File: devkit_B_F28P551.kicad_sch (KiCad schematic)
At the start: 27 parts, among them J1 DEVKIT_C2000_ROW_A, J2 DEVKIT_C2000_ROW_B, J3 Tag-Connect-2050_10, J4 RESET, U1 TMS320F28P551SG5PM, U2 MCP1700-3302E/TT, U3 MCP1700-3302E/TT

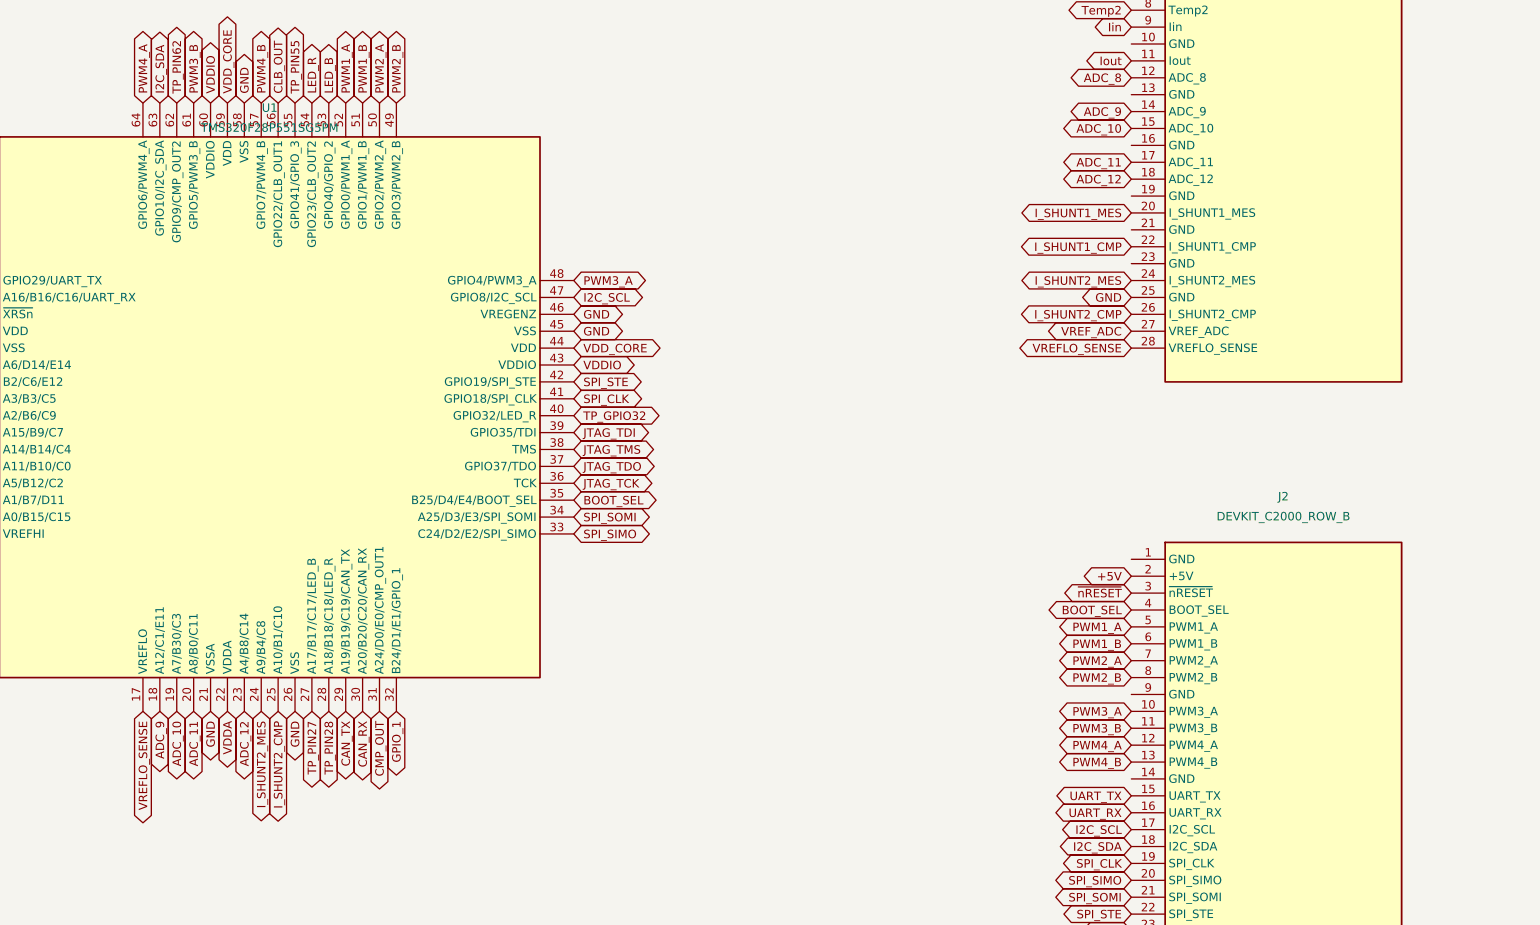
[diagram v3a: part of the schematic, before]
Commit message: Renseigne les empreintes manquantes sur J1, J2, J3 et U1
« Mettre a jour le PCB depuis le schema » a pose 23 empreintes sur 26 et
refuse les trois plus importantes: le MCU et les deux rangees du connecteur.
Cause: KiCad lit la propriete Footprint de l'INSTANCE, pas celle de la
librairie, et les schemas importes la portaient vide — ou pas du tout.

Les deux formats coexistent dans le depot et demandaient deux traitements:
KiCad 10 ecrit une propriete Footprint vide qu'il suffit de remplir, KiCad 8
n'en ecrit aucune et il faut l'inserer.

Le cache (lib_symbols) du schema n'etait pas une source fiable non plus:
plusieurs symboles y avaient perdu leur empreinte alors que la librairie la
porte. gen_empreintes.py lit donc sym-lib-table et fait primer la librairie.

ERC inchange sur les deux cartes.

Co-Authored-By: Claude Opus 5 <noreply@anthropic.com>
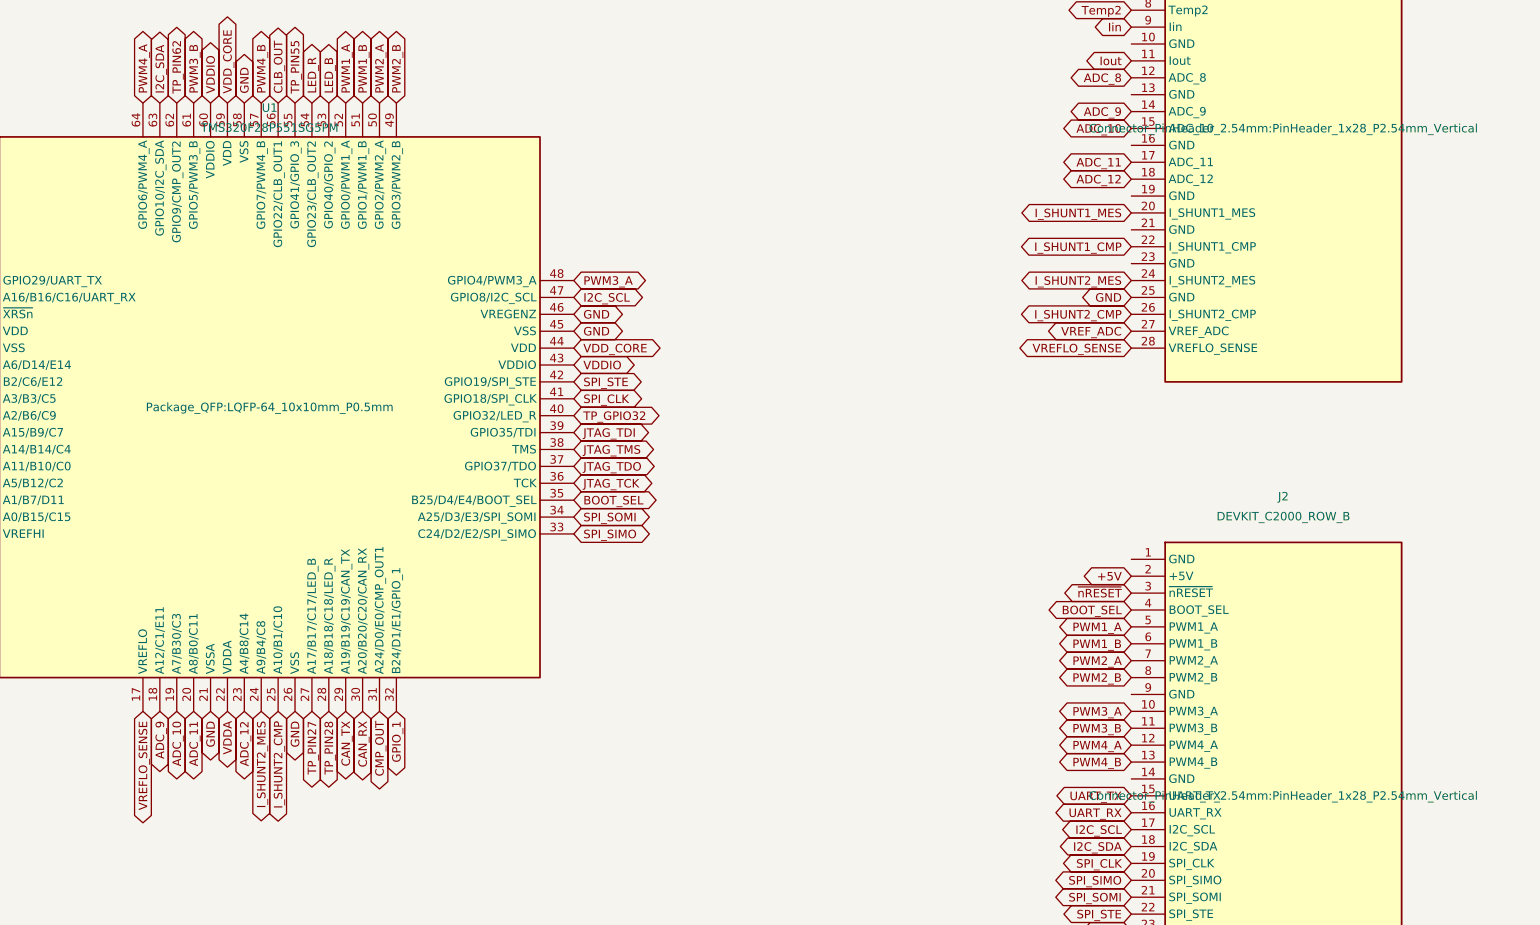
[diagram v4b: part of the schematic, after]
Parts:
- J1, J2: footprint (none) -> Connector_PinHeader_2.54mm:PinHeader_1x28_P2.54mm_Vertical
- U1: footprint (none) -> Package_QFP:LQFP-64_10x10mm_P0.5mm
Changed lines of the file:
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@@
 			)
 		)
-		(property "Footprint" ""
+		(property "Footprint" "Connector_PinHeader_2.54mm:PinHeader_1x28_P2.54mm_Vertical"
 			(at 279.4 59.69 0)
 			(show_name no)
@@
 			)
 		)
-		(property "Footprint" ""
+		(property "Footprint" "Connector_PinHeader_2.54mm:PinHeader_1x28_P2.54mm_Vertical"
 			(at 279.4 160.02 0)
 			(show_name no)
@@
 			)
 		)
-		(property "Footprint" ""
+		(property "Footprint" "Package_QFP:LQFP-64_10x10mm_P0.5mm"
 			(at 127 101.6 0)
 			(show_name no)
